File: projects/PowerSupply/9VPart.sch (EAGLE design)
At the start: 26 parts, among them IC1 LM2596T, IC2 LM2596T, X1 IN, X2 OUT

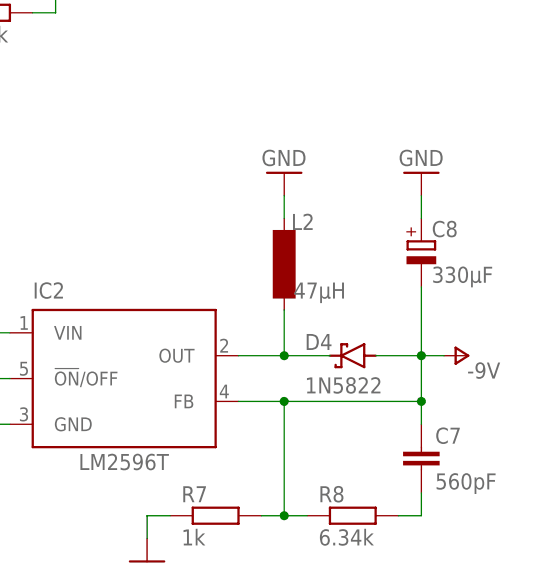
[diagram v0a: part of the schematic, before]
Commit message: feat: 9 volt part modified
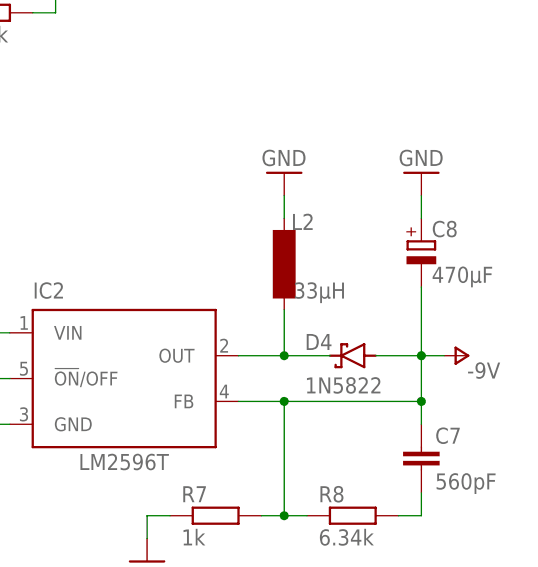
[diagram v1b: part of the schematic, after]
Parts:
- C8: value 330µF -> 470µF
- L1: device inductor-neosid:SD12-680 -> bb84:IND-120-330K
- L2: value 47µH -> 33µH; device inductor-neosid:SD12-680 -> bb84:IND-120-330K
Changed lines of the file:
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@@
 <part name="D2" library="diode" library_urn="urn:adsk.eagle:library:210" deviceset="SCHOTTKY-DIODE" device="C4111-15" package3d_urn="urn:adsk.eagle:package:43355/2" value="1N5822"/>
 <part name="GND5" library="supply1" library_urn="urn:adsk.eagle:library:371" deviceset="GND" device=""/>
-<part name="L1" library="inductor-neosid" library_urn="urn:adsk.eagle:library:241" deviceset="SD12" device="-680" package3d_urn="urn:adsk.eagle:package:14657/1" value="33µH"/>
+<part name="L1" library="bb84" deviceset="IND-120-330K" device="" value="33µH"/>
 <part name="C4" library="rcl" library_urn="urn:adsk.eagle:library:334" deviceset="CPOL-EU" device="E3.5-8" package3d_urn="urn:adsk.eagle:package:23360/2" value="220µF"/>
 <part name="X2" library="con-wago-508" library_urn="urn:adsk.eagle:library:196" deviceset="W237-03P" device="" package3d_urn="urn:adsk.eagle:package:10737/1" value="OUT"/>
 <part name="GND7" library="supply1" library_urn="urn:adsk.eagle:library:371" deviceset="GND" device=""/>
 <part name="IC2" library="national-semiconductor" library_urn="urn:adsk.eagle:library:307" deviceset="LM2596" device="T" package3d_urn="urn:adsk.eagle:package:21216/1"/>
-<part name="L2" library="inductor-neosid" library_urn="urn:adsk.eagle:library:241" deviceset="SD12" device="-680" package3d_urn="urn:adsk.eagle:package:14657/1" value="47µH"/>
+<part name="L2" library="bb84" deviceset="IND-120-330K" device="" value="33µH"/>
 <part name="GND9" library="supply1" library_urn="urn:adsk.eagle:library:371" deviceset="GND" device=""/>
 <part name="D4" library="diode" library_urn="urn:adsk.eagle:library:210" deviceset="SCHOTTKY-DIODE" device="C4111-15" package3d_urn="urn:adsk.eagle:package:43355/2" value="1N5822"/>
-<part name="C8" library="rcl" library_urn="urn:adsk.eagle:library:334" deviceset="CPOL-EU" device="E3.5-8" package3d_urn="urn:adsk.eagle:package:23360/2" value="330µF"/>
+<part name="C8" library="rcl" library_urn="urn:adsk.eagle:library:334" deviceset="CPOL-EU" device="E3.5-8" package3d_urn="urn:adsk.eagle:package:23360/2" value="470µF"/>
 <part name="R7" library="rcl" library_urn="urn:adsk.eagle:library:334" deviceset="R-EU_" device="0207/10" package3d_urn="urn:adsk.eagle:package:23491/2" value="1k"/>
 <part name="R8" library="rcl" library_urn="urn:adsk.eagle:library:334" deviceset="R-EU_" device="0207/10" package3d_urn="urn:adsk.eagle:package:23491/2" value="6.34k"/>
